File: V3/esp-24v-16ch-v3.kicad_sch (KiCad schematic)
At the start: 4 parts, among them J3 DB141V-2.54-8P, J4 DB141V-2.54-8P, J5 DB141V-2.54-8P, J6 DB141V-2.54-8P

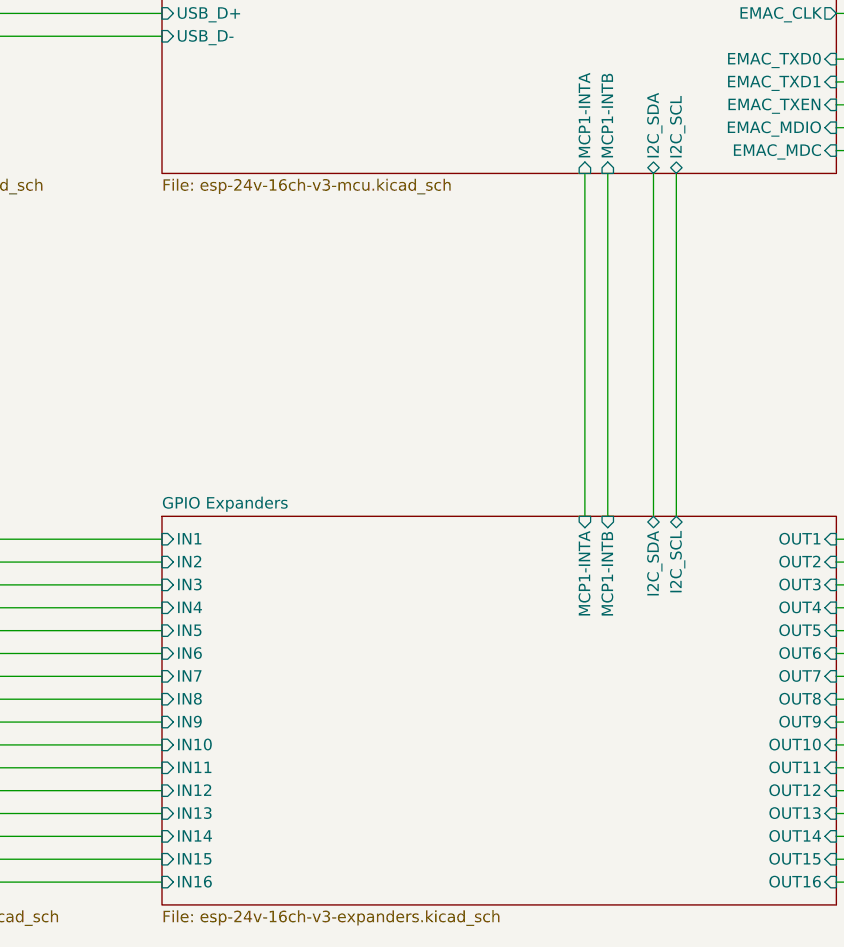
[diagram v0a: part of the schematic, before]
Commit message: Added NTC inputs and redone routing
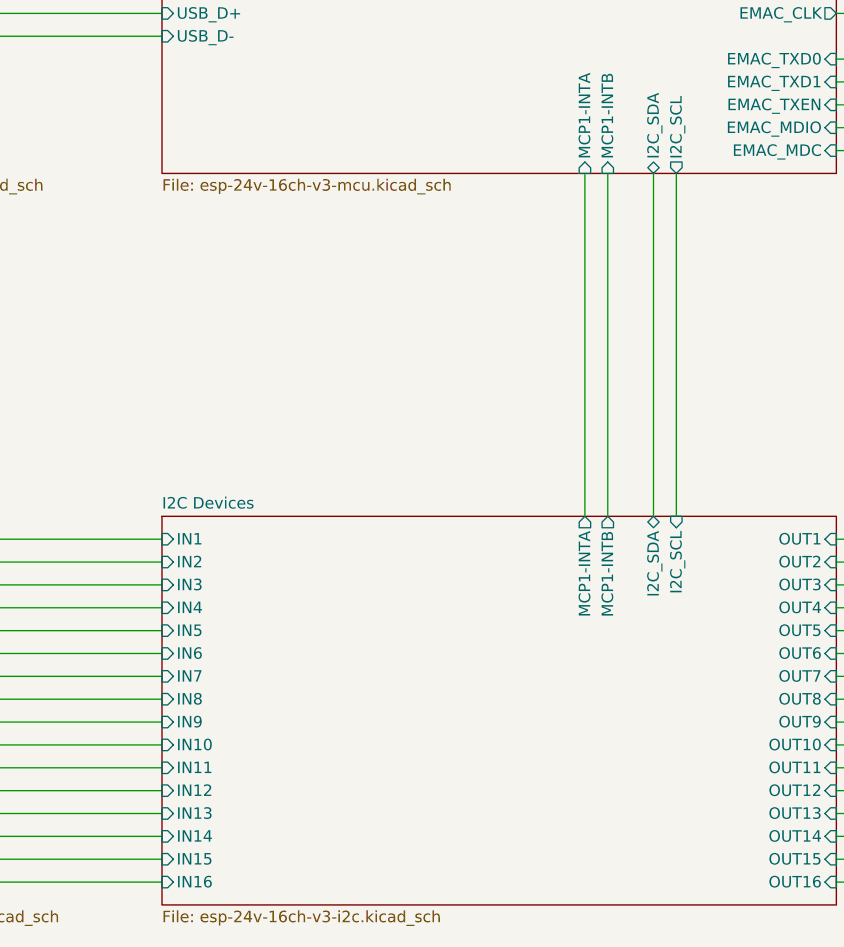
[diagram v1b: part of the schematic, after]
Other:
- sheet GPIO Expanders renamed I2C Devices
- sheet I2C Devices: file esp-24v-16ch-v3-expanders.kicad_sch -> esp-24v-16ch-v3-i2c.kicad_sch
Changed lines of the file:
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@@
 			(color 0 0 0 0.0000)
 		)
-		(property "Sheetname" "GPIO Expanders"
+		(property "Sheetname" "I2C Devices"
 			(at 110.49 91.9984 0)
 			(effects
@@
 			)
 		)
-		(property "Sheetfile" "esp-24v-16ch-v3-expanders.kicad_sch"
+		(property "Sheetfile" "esp-24v-16ch-v3-i2c.kicad_sch"
 			(at 110.49 136.4746 0)
 			(effects
@@
 			)
 		)
-		(pin "I2C_SCL" bidirectional
+		(pin "I2C_SCL" input
 			(at 167.64 92.71 90)
 			(effects
@@
 			)
 		)
-		(pin "MCP1-INTB" input
+		(pin "MCP1-INTB" output
 			(at 160.02 92.71 90)
 			(effects
@@
 			)
 		)
-		(pin "MCP1-INTA" input
+		(pin "MCP1-INTA" output
 			(at 157.48 92.71 90)
 			(effects
@@
 			)
 		)
-		(pin "I2C_SCL" bidirectional
+		(pin "I2C_SCL" output
 			(at 167.64 54.61 270)
 			(effects

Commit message: Renamed to V3.2
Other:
- title: ESP 16x 24VDC Input 16x 24VDC Output Module -> ESP 24V 16xIn/16xOut/4xNTC Module
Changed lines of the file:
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@@
 	(paper "A4")
 	(title_block
-		(title "ESP 16x 24VDC Input 16x 24VDC Output Module")
-		(date "2024-11-06")
-		(rev "V3")
+		(title "ESP 24V 16xIn/16xOut/4xNTC Module")
+		(date "2025-06-29")
+		(rev "V3.2")
 	)
 	(wire
@@
 			(project "esp-24v-16ch-v3"
 				(path "/2bc5a21a-1d79-419d-a592-6852cc07b00a"
-					(page "8")
-				)
-			)
+					(page "7")
+				)
+			)
